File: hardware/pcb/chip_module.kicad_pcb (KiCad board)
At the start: 4 copper layers, 150 x 140 mm, 200 parts, among them J12 BTB_DAUGHTER

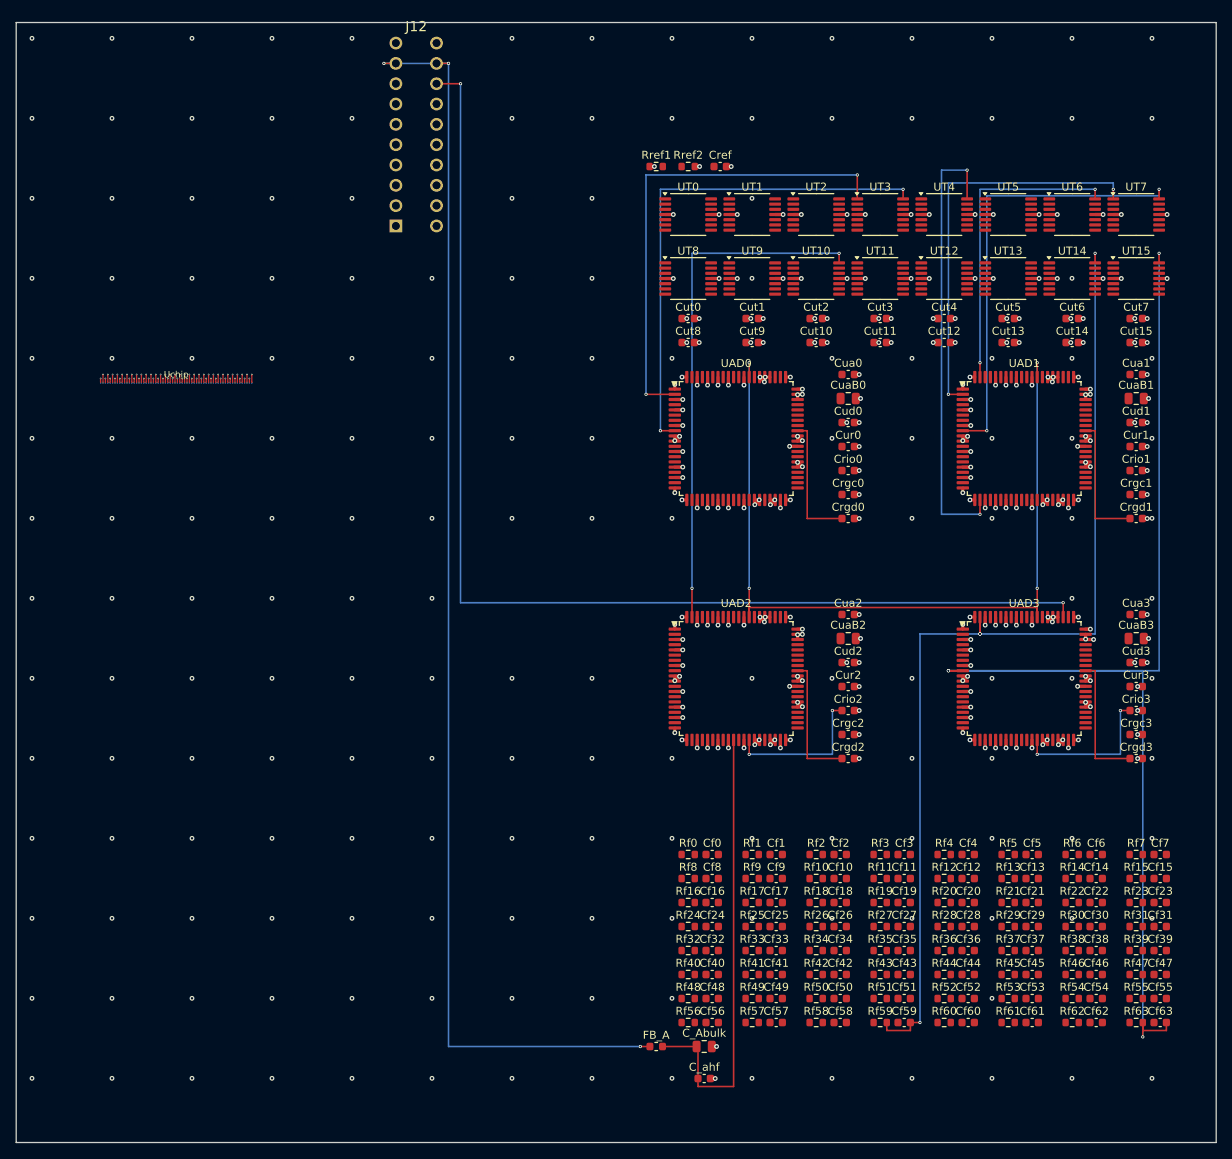
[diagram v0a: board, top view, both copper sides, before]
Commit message: pcb: Ironwood SBT socket + per-datasheet pin fixes + no_connect markers
Step 0 — Ironwood SBT open-top spring-pin socket (emitter face, main board):
  - socket_footprint(): 65 solder pads (64 EM + EM_ANODE) on F.Cu+F.Paste+F.Mask
    at the 0.30mm die-contact pitch, 4 NPTH M2 mount holes, 25x25mm body +
    courtyard. lib_id "qssc:Ironwood_SBT" + symbol; Uchip swapped from
    QSSC_Chip_EM. This is the commercial made-to-order socket that fits the
    20x20mm / 0.30mm-pitch die (no off-the-shelf socket exists at that pitch).
  - Head-board QSSC_Chip_DET (detector face) unchanged: ACF/pogo on B.Cu.

Step 1 — per-datasheet pin audit + (no_connect) emission (addresses
"practically nothing connected per its datasheet"):
  - FT232RL: net pin 24 -> +3V3 (VCC) and pin 23 -> GND (AGND) -- both required
    supply/ground pads per SSOP-28 that were previously unnetted.
  - ADF4351: REFIN- (pin 19) decoupled to GND via new C37 100nF (single-ended
    CMOS ref, datasheet Fig.51); unused RFOUTB+/- (13,14), RFOUTA- (15), SW (5),
    CE (25) declared no_connect per datasheet (unused RF outputs float).
  - add() now takes nc_pins=...; emit_schematic() emits (no_connect) sexps at
    every documented-unused pin: FT232 modem/crystal/LED (12 pins), ADF4351 (5),
    AD7616 parallel-DB bus + SDI/SDOB in 1-wire HW mode (10/chip x4 = 40 head),
    TLC5947 chip2 OUT16-23 + SOUT (9 main).

Both boards: DRC 0/0/0, ERC 0 errors / 0 warnings. 9 PCB tests green.

Co-Authored-By: Claude Code <noreply@anthropic.com>
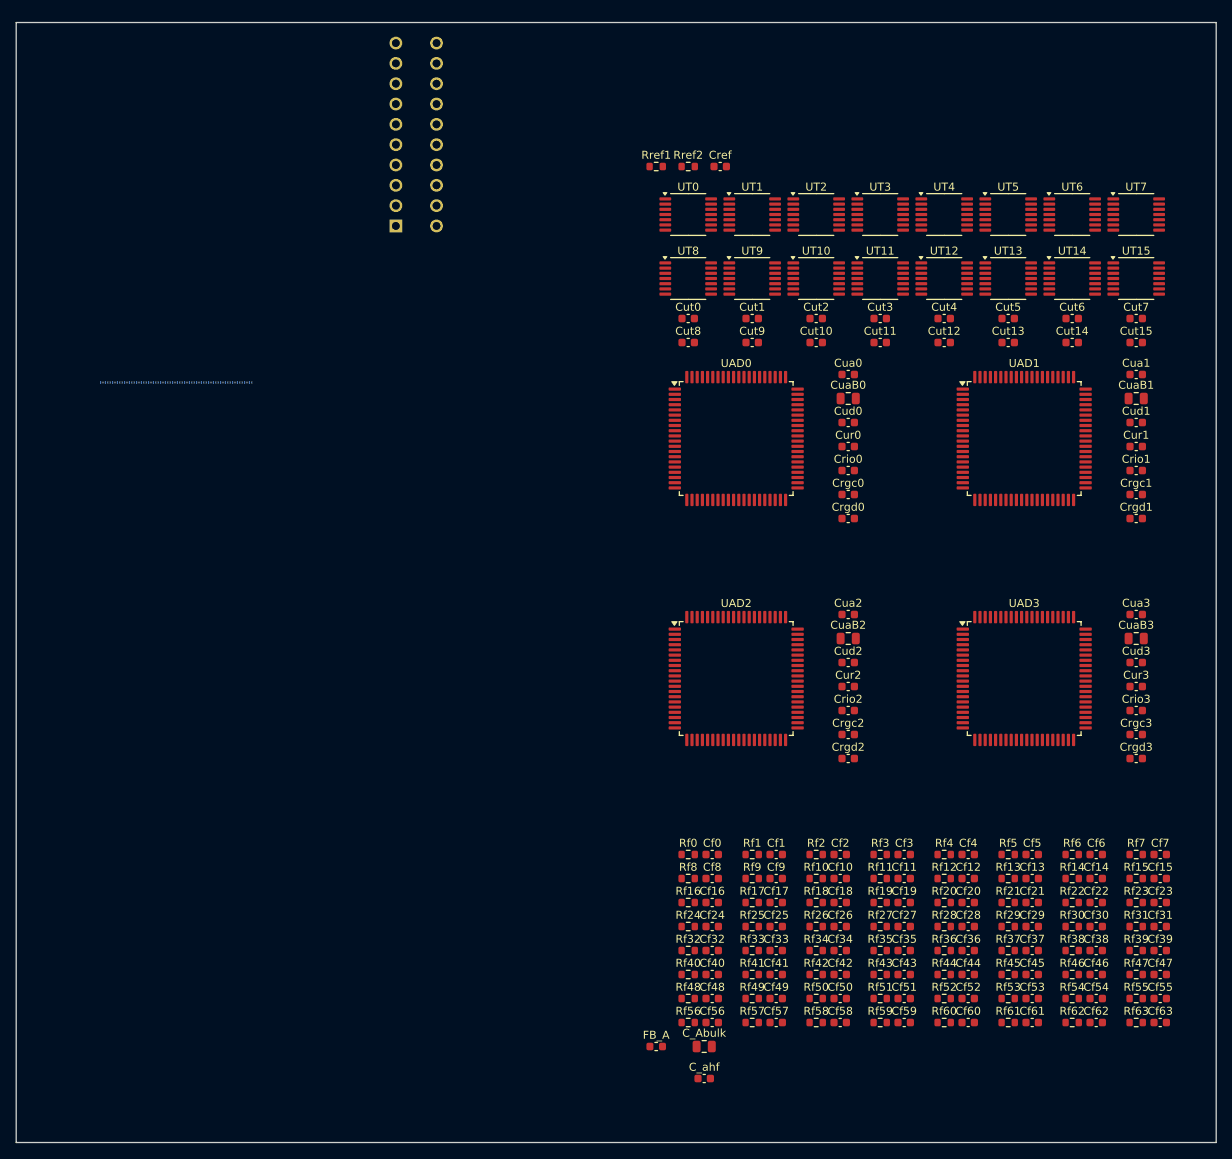
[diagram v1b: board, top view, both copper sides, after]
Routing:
- net GND: track 162.8 -> 0.00 mm, vias 382 -> 0
- net DET_TIA63: track 160.1 -> 0.00 mm, vias 4 -> 0
- net +5V: track 159.1 -> 0.00 mm, vias 3 -> 0
- net adc_cs3: track 145.0 -> 0.00 mm, vias 2 -> 0
- net DET_TIA59: track 129.6 -> 0.00 mm, vias 4 -> 0
- net adc_convst: track 105.6 -> 0.00 mm, vias 4 -> 0
- net DET_TIA43: track 65.1 -> 0.00 mm, vias 2 -> 0
- net DET_TIA15: track 63.5 -> 0.00 mm, vias 2 -> 0
- net DET_TIA12: track 60.4 -> 0.00 mm, vias 2 -> 0
- net +5V_A: track 57.2 -> 0.00 mm
- net DET_TIA19: track 56.4 -> 0.00 mm, vias 2 -> 0
- net DET_TIA31: track 55.9 -> 0.00 mm, vias 2 -> 0
- net DET_TIA28: track 50.8 -> 0.00 mm, vias 2 -> 0
- net +3V3: track 40.8 -> 0.00 mm, vias 53 -> 0
- net DET_TIA27: track 39.1 -> 0.00 mm, vias 2 -> 0
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- removed copper zone on In2.Cu, net +3V3
- removed copper zone on In1.Cu, net GND

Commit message: pcb: verify netlist complete per datasheets, fix C_in/C37 placement short
Connection audit (tools/audit_connections.py) confirms both boards are
netlist-complete and datasheet-correct BEFORE routing:

  - ERC: 0 errors both boards (qssc + chip_module). The 145/203 remaining
    messages are all endpoint_off_grid warnings (authored symbols on a
    non-1.27 mm pin grid) -- cosmetic noise.
  - DRC: 0 violations, 0 unconnected pads, 0 footprint errors both boards.
  - Chip die: 64 emitter_cat -> TLC5947 OUT sinks + EM_ANODE -> +12V_EMIT
    on the main board; 64 DET_IN -> TLV9004 TIA -> AD7616 + DET_REF on the
    head. Every chip net has an off-chip destination (audit confirms).
  - All 268 main-board + head "unnetted" IC pins are intentional spares,
    not missing connections: FPGA 185 spare IO balls (99 power balls all
    netted), AD7616 parallel-DB bus + SDI/SDOB in 1-wire HW serial mode,
    FT232 modem/CBUS pins (USB-only; pin 23 AGND + 24 VCC ARE netted),
    ADF4351 NC pins 5/13/14/15/25 per datasheet, TLC5947 chip2 unused
    OUT16-23 + SOUT, and numberless EP/mount-hole cosmetic pads.

Fix: the main board had 3 DRC violations (shorting_items +5V_IN/ADF_TEMP,
courtyards_overlap, solder_mask_bridge) all from ONE root cause -- the new
input-bulk cap C_in and the ADF4351 TEMP decoupler C37 both fell through
assign_pcb_positions()'s else-branch to the (50,50) default cell, so
C_in.1 (+5V_IN) overlapped C37.1 (ADF_TEMP). Give both explicit placements
in the fixed dict (C_in @46,8 near the barrel jack; C37 @104,36 below U3).
Regenerated both boards -> DRC 0/0/0.

route_signals.py: the chip-net force-fail referenced an undefined
`structured_chip` (NameError if run). Define it as an empty set so the
file is runnable and all chip nets are cleanly deferred to the future
_structured_bus_fanout (task #36) / FreeRouting -- routing stays paused
per the user's instruction until the netlist was verified.

Adds tools/audit_connections.py (per-datasheet pin/rail/chip audit) a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
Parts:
- added C_5V: 10uF, C_0805_2012Metric, F.Cu at (20.0, 70.0)
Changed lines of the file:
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@@
+		)
+	)
+	(footprint "C_0805_2012Metric"
+		(version 20240108)
+		(generator "pcbnew")
+		(generator_version "8.0")
+		(layer "F.Cu")
+		(at 20 70 0)
+		(descr "Capacitor SMD 0805 (2012 Metric), square (rectangular) end terminal, IPC_7351 nominal, (Body size source: IPC-SM-782 page 76, https://www.pcb-3d.com/wordpress/wp-content/uploads/ipc-sm-782a_amendment_1_and_2.pdf, https://docs.google.com/spreadsheets/d/1BsfQQcO9C6DZCsRaXUlFlo91Tg2WpOkGARC1WS5S8t0/edit?usp=sharing), generated with kicad-footprint-generator")
+		(tags "capacitor")
+		(property "Reference" "C_5V"
+			(at 0 -1.68 0)
+			(layer "F.SilkS")
+			(effects
+				(font
+					(size 1 1)
+					(thickness 0.15)
+				)
+			)
+		)
+		(property "Value" "10uF"
+			(at 0 1.68 0)
+			(layer "F.Fab")
+			(effects
+				(font
+					(size 1 1)
+					(thickness 0.15)
+				)
+			)
+		)
+		(property "Footprint" ""
+			(at 0 0 0)
+			(unlocked yes)
+			(layer "F.Fab")
+			(hide yes)
+			(effects
+				(font
+					(size 1.27 1.27)
+				)
+			)
+		)
+		(property "Datasheet" ""
+			(at 0 0 0)
+			(unlocked yes)
+			(layer "F.Fab")
+			(hide yes)
+			(effects
+				(font
+					(size 1.27 1.27)
+				)
+			)
+		)
+		(property "Description" ""
+			(at 0 0 0)
+			(unlocked yes)
+			(layer "F.Fab")
+			(hide yes)
+			(effects
+				(font
+					(size 1.27 1.27)
+				)
+			)
+		)
+		(attr smd)
+		(fp_line
+			(start -0.261252 -0.735)
+			(end 0.261252 -0.735)
+			(stroke
+				(width 0.12)
+				(type solid)
+			)
+			(layer "F.SilkS")
+		)
+		(fp_line
+			(start -0.261252 0.735)
+			(end 0.261252 0.735)
+			(stroke
+				(width 0.12)
+				(type solid)
+			)
+			(layer "F.SilkS")
+		)
+		(fp_line
+			(start -1.7 -0.98)
+			(end 1.7 -0.98)
+			(stroke
+				(width 0.05)
+				(type solid)
+			)
+			(layer "F.CrtYd")
+		)
+		(fp_line
+			(start -1.7 0.98)
+			(end -1.7 -0.98)
+			(stroke
+				(width 0.05)
+				(type solid)
+			)
+			(layer "F.CrtYd")
+		)
+		(fp_line
+			(start 1.7 -0.98)
+			(end 1.7 0.98)
+			(stroke
+				(width 0.05)
+				(type solid)
+			)
+			(layer "F.CrtYd")
+		)
+		(fp_line
+			(start 1.7 0.98)
+			(end -1.7 0.98)
+			(stroke
+				(width 0.05)
+				(type solid)
+			)
+			(layer "F.CrtYd")
+		)
+		(fp_line
+			(start -1 -0.625)
+			(end 1 -0.625)
+			(stroke
+				(width 0.1)
+				(type solid)
+			)
+			(layer "F.Fab")
+		)
+		(fp_line
+			(start -1 0.625)
+			(end -1 -0.625)
+			(stroke
+				(width 0.1)
+				(type solid)
+			)
+			(layer "F.Fab")
+		)
+		(fp_line
+			(start 1 -0.625)
+			(end 1 0.625)
+			(stroke
+				(width 0.1)
+				(type solid)
+			)
+			(layer "F.Fab")
+		)
+		(fp_line
+			(start 1 0.625)
+			(end -1 0.625)
+			(stroke
+				(width 0.1)
+				(type solid)
+			)
+			(layer "F.Fab")
+		)
+		(fp_text user "${REFERENCE}"
+			(at 0 0 0)
+			(layer "F.Fab")
+			(effects
+				(font
+					(size 0.5 0.5)
+					(thickness 0.08)
+				)
+			)
+		)
+		(pad "1" smd roundrect
+			(at -0.95 0)
+			(size 1 1.45)
+			(layers "F.Cu" "F.Paste" "F.Mask")
+			(net 2 "+5V")
+			(roundrect_rratio 0.25)
+		)
+		(pad "2" smd roundrect
+			(at 0.95 0)
+			(size 1 1.45)
+			(layers "F.Cu" "F.Paste" "F.Mask")
+			(net 133 "GND")
+			(roundrect_rratio 0.25)
+		)
+		(model "${KICAD8_3DMODEL_DIR}/Capacitor_SMD.3dshapes/C_0805_2012Metric.wrl"
+			(offset
+				(xyz 0 0 0)
+			)
+			(scale
+				(xyz 1 1 1)
+			)
+			(rotate
+				(xyz 0 0 0)
+			)
 		)
 	)

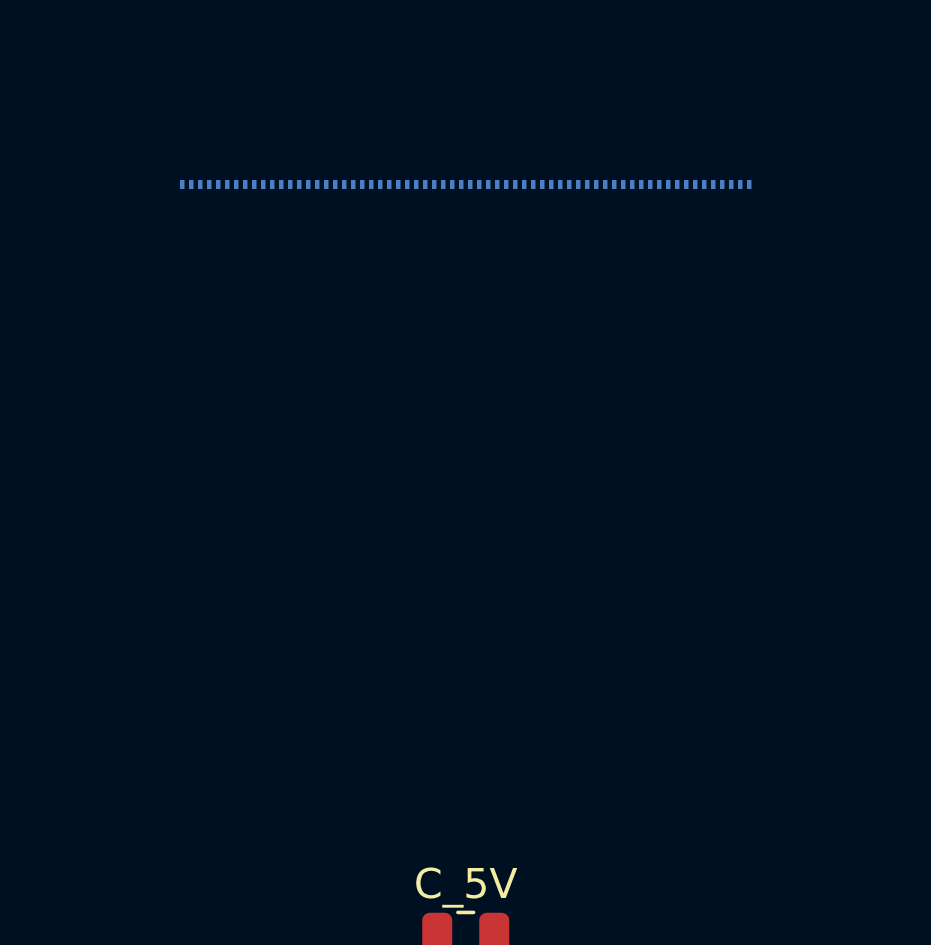
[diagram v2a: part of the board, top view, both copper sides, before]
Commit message: pcb: fix die electrode geometry -- 8x8 grid across 20x20 mm face (2.5 mm pitch)
The optical die carries an 8x8 grid of electrodes = 64 pads evenly across the
2x2 cm (20x20 mm) face (~2.5 mm pitch), NOT a 1x64 perimeter row at 0.30 mm.
The count (64) and net assignments were already correct, but the footprint pad
GEOMETRY was wrong: chip_footprint_em/det + socket_footprint placed all 64 pads
in a single row along one edge at 0.30 mm pitch. The user (die spec author)
corrected this: "el chip optico tiene 8 x 8 electrodos en 2 cm x 2 cm".

Replace _PITCH/_X0 (0.30 mm perimeter row) with an 8x8 grid:
  GRID_N=8, GRID_PITCH=2.5 mm, _chip_grid_xy(i) -> row-major (row=i//8,
  col=i%8) centered on the 20x20 mm die (grid spans -8.75..+8.75 mm in x,y).
  EM0/DET0 -> top-left (-8.75,-8.75); EM63 -> bottom-right (+8.75,+8.75).
  Pad size 1.2x1.2 mm (1.3 mm gap at 2.5 mm pitch -- comfortable for ACF /
  socket contact).  EM_ANODE common-anode pad stays on the LEFT edge at
  (-9.9, 0), clear of the grid's leftmost column (x=-8.75).

Applied to all three die footprints: QSSC_Chip_EM (ACF emitter face),
QSSC_Chip_DET (ACF detector face, B.Cu), Ironwood_SBT (soldered socket,
F.Cu+F.Paste+F.Mask).  Schematic pin lists unchanged (independent 1.0 mm
symbol grid -- connectivity is by name, not geometry).

Verified: both boards DRC 0/0/0, ERC 0 errors; MAIN Ironwood_SBT 65/65 pads
netted (64 EM + EM_ANODE), HEAD QSSC_Chip_DET 64/64 netted.  4 PCB tests pass
(router _chip_fanout is pad-layer-derived and adapts to the new positions).

Co-Authored-By: Claude Code <noreply@anthropic.com>
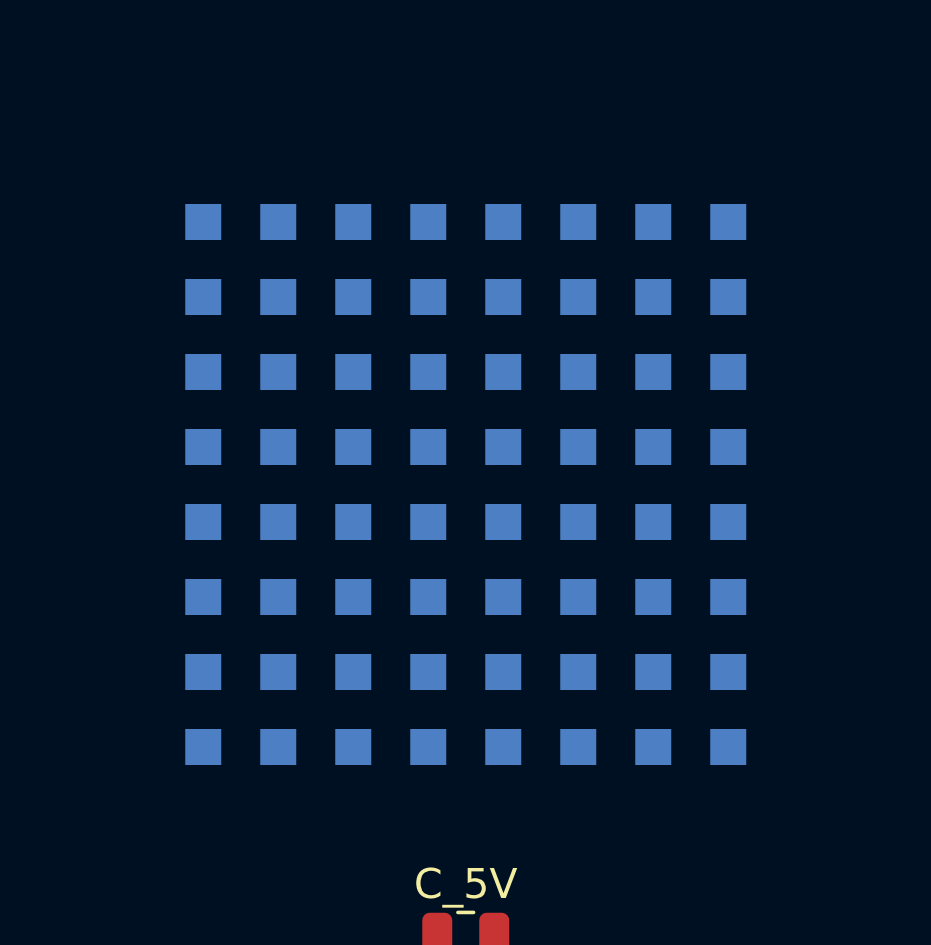
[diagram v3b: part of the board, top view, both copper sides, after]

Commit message: route: make _chip_fanout a no-op for the 2.5 mm 8x8 die grid (FreeRouting escapes)
The 8x8 die electrode grid is 2.5 mm pitch (1.2 mm pads, 1.3 mm inter-pad
gaps) -- COARSE, not the 0.30 mm fine pitch the staggered dog-bone fanout was
written for. Applying that dog-bone geometry to an INTERIOR 8x8 grid shorts
neighbouring nets: each pad's per-pad escape direction (nearest die edge) lands
its 0.5/1.0 mm stub+via on the adjacent-row pad -> DRC shorting_items between
emitter_cat{i} and emitter_cat{i+8} (68 shorts main / 98 head after routing).

At 2.5 mm pitch a 0.2 mm track escapes each pad directly through the 1.3 mm
gaps, so no dog-bone vias are needed. _chip_fanout is now a no-op (returns the
empty 5-tuple); the 64 die nets stay bare and force-failed in the line router,
and FreeRouting escapes the 8x8 grid directly -- a standard autorouter job at
this pitch. Verified: both boards DRC 0 violations after route_signals
(was 68/98 shorting_items). Die nets (64 emitter_cat / 64 DET_IN+DET_TIA) +
signal nets remain unrouted, pending the FreeRouting pass.

Co-Authored-By: Claude Code <noreply@anthropic.com>
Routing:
- net +5V: track 0.00 -> 225.5 mm, vias 0 -> 4
- net adc_convst: track 0.00 -> 210.0 mm, vias 0 -> 6
- net DET_TIA63: track 0.00 -> 160.1 mm, vias 0 -> 4
- net adc_cs3: track 0.00 -> 145.0 mm, vias 0 -> 2
- net DET_TIA59: track 0.00 -> 133.2 mm, vias 0 -> 4
- net adc_cs0: track 0.00 -> 81.6 mm, vias 0 -> 2
- net +5V_A: track 0.00 -> 57.2 mm
- net adc_refio3: track 0.00 -> 18.9 mm, vias 0 -> 2
- net adc_refio2: track 0.00 -> 18.9 mm, vias 0 -> 2
- net adc_rgd0: track 0.00 -> 16.5 mm
- net adc_rgd2: track 0.00 -> 16.5 mm
- net adc_rgd1: track 0.00 -> 16.5 mm
- net adc_rgd3: track 0.00 -> 16.5 mm
